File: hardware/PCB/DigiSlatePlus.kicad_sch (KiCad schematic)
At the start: 37 parts, among them J1 Serial, J2 USB_B, J6 Mains, J7 Timecode IN, J8 Timecode OUT, Q4 2N2222, SW1 RotaryEncoder-SW, SW2 1, SW3 1, SW4 1, SW5 1, U1 ESP32-S3-WROOM-1, U2 DS3231M

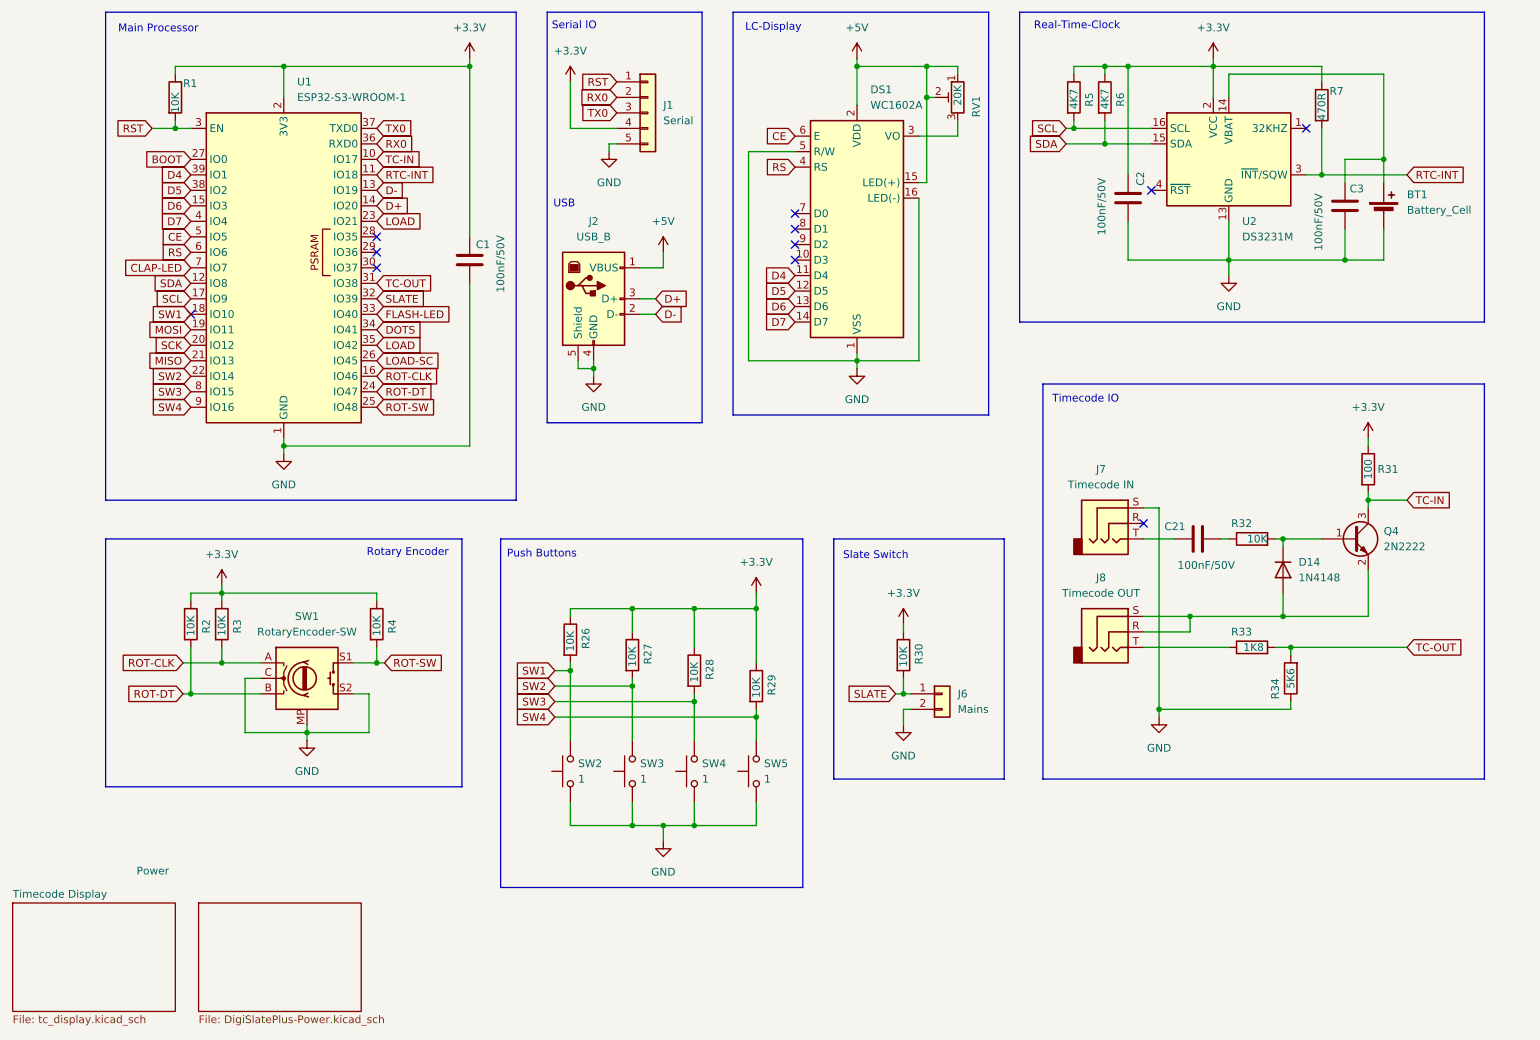
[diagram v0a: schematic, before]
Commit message: first finished schematic version
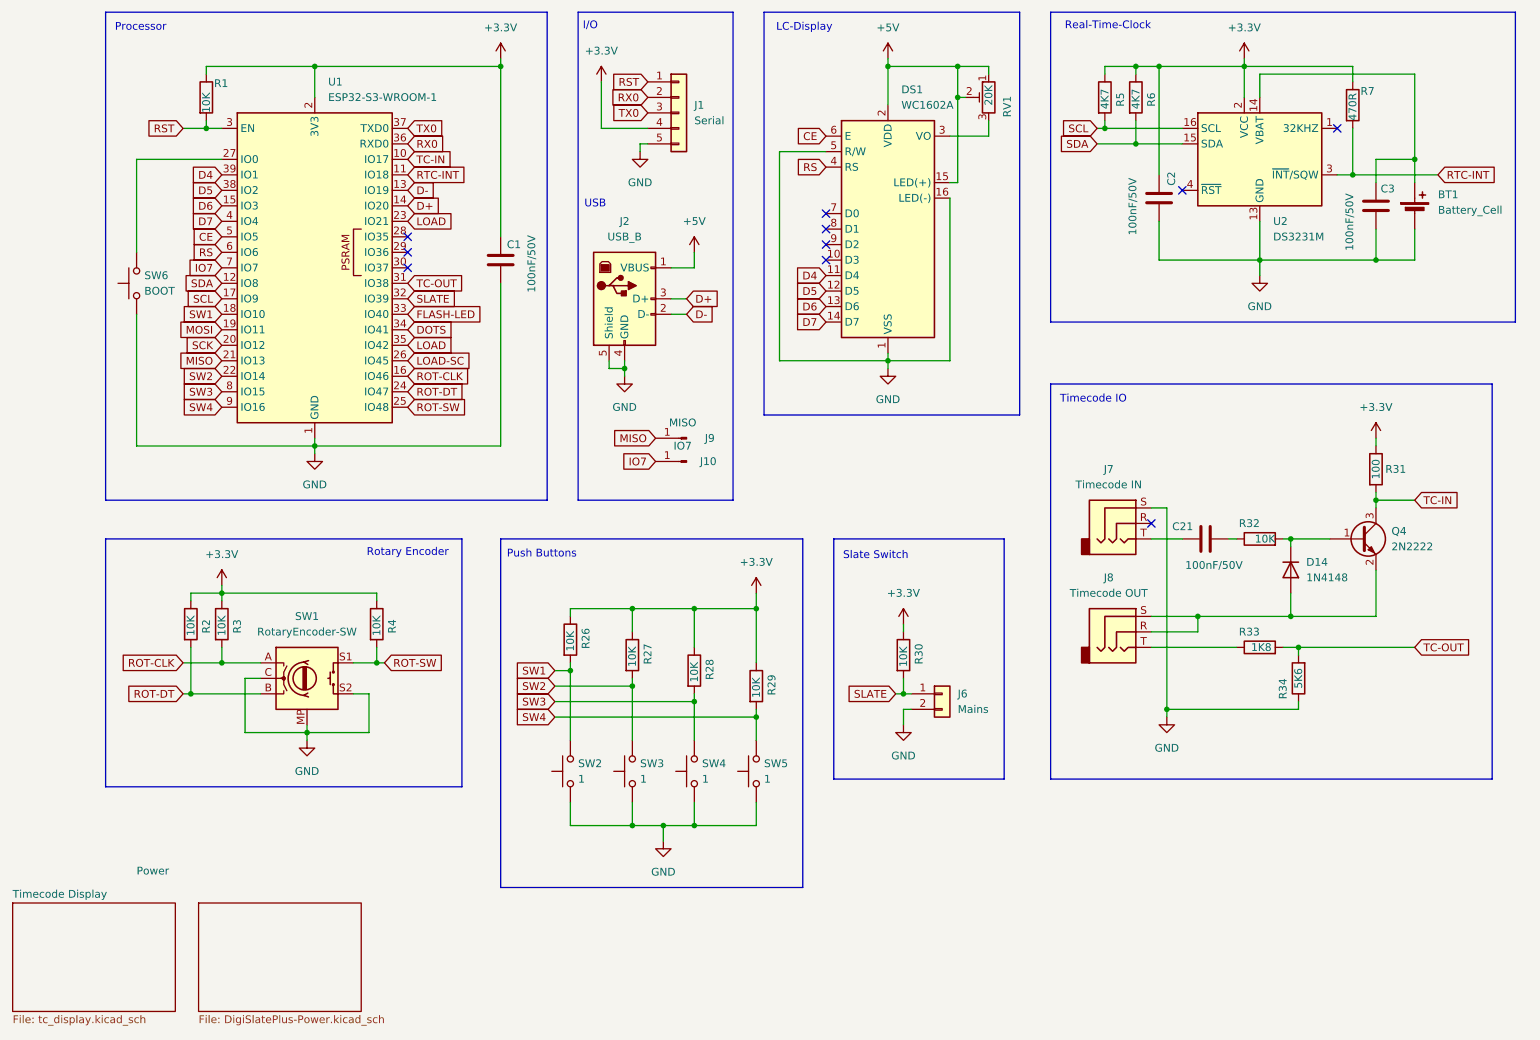
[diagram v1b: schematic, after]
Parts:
- added J10: IO7, Connector_PinHeader_1.00mm:PinHeader_1x01_P1.00mm_Vertical, symbol Connector:Conn_01x01_Pin
- added J9: MISO, Connector_PinHeader_1.00mm:PinHeader_1x01_P1.00mm_Vertical, symbol Connector:Conn_01x01_Pin
- added SW6: BOOT, Button_Switch_SMD:SW_Push_SPST_NO_Alps_SKRK, symbol Switch:SW_Push
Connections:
- net GND: now also SW6.1
- net MISO: now also J9.1 (Pin_1)
- net BOOT: no longer names the net of U1.27 (IO0)
- net BOOT: now also SW6.2
- net CLAP-LED renamed IO7
- net IO7: now also J10.1 (Pin_1)
- no-connect marks 11 -> 10
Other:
- note added: "I/O"
- note added: "Processor"
- note removed: "Main Processor"
- note removed: "Serial IO"
- moved on the sheet: BT1, C1, C2, C21, C3, D14, DS1, J1, J2, J7, J8, Q4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

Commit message: final 1.0 board version
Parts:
- SW2, SW3, SW4, SW5: footprint Button_Switch_THT:SW_PUSH-12mm -> Button_Switch_THT:SW_Tactile_Straight_KSA0Axx1LFTR
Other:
- sheet Timecode Display renamed Display
- title: DigiSlatePlus -> DigiSlate+
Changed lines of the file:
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@@
 	(paper "A4")
 	(title_block
-		(title "DigiSlatePlus")
+		(title "DigiSlate+")
+		(date "2024-09-05")
 		(rev "1.0")
 	)
@@
 			)
 		)
-		(property "Footprint" "Button_Switch_THT:SW_PUSH-12mm"
+		(property "Footprint" "Button_Switch_THT:SW_Tactile_Straight_KSA0Axx1LFTR"
 			(at 114.3 152.4 0)
 			(effects
@@
 			)
 		)
-		(property "Footprint" "Button_Switch_THT:SW_PUSH-12mm"
+		(property "Footprint" "Button_Switch_THT:SW_Tactile_Straight_KSA0Axx1LFTR"
 			(at 124.46 152.4 0)
 			(effects
@@
 			)
 		)
-		(property "Footprint" "Button_Switch_THT:SW_PUSH-12mm"
+		(property "Footprint" "Button_Switch_THT:SW_Tactile_Straight_KSA0Axx1LFTR"
 			(at 104.14 152.4 0)
 			(effects
@@
 			)
 		)
-		(property "Footprint" "Button_Switch_THT:SW_PUSH-12mm"
+		(property "Footprint" "Button_Switch_THT:SW_Tactile_Straight_KSA0Axx1LFTR"
 			(at 134.62 152.4 0)
 			(effects
@@
 			(color 0 0 0 0.0000)
 		)
-		(property "Sheetname" "Timecode Display"
+		(property "Sheetname" "Display"
 			(at 17.78 173.2784 0)
 			(effects
@@
 		)
 		(property "Sheetname" "Power"
-			(at 38.1 169.4684 0)
+			(at 48.006 172.974 0)
 			(effects
 				(font
